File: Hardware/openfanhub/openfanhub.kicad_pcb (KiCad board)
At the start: 2 copper layers, 39.9 x 83.8 mm, 25 parts, among them J1 Conn_01x04_Male, J10 Conn_01x04_Male, J11 Conn_01x04_Male, J12 Conn_01x04_Male, J13 Conn_01x04_Male, J14 Conn_01x04_Male, J15 Conn_01x04_Male, J2 Conn_01x04_Male, J3 Conn_01x04_Male, J4 Conn_01x04_Male, J5 Conn_01x04_Male, J6 Conn_01x04_Male, J7 Conn_01x04_Male, J8 Conn_01x04_Male, J9 Conn_01x04_Male, U1 STM32F103C8T8_Board, U2 AMS1117, U3 USB_HEADER_IN, U4 USB_HEADER_OUT

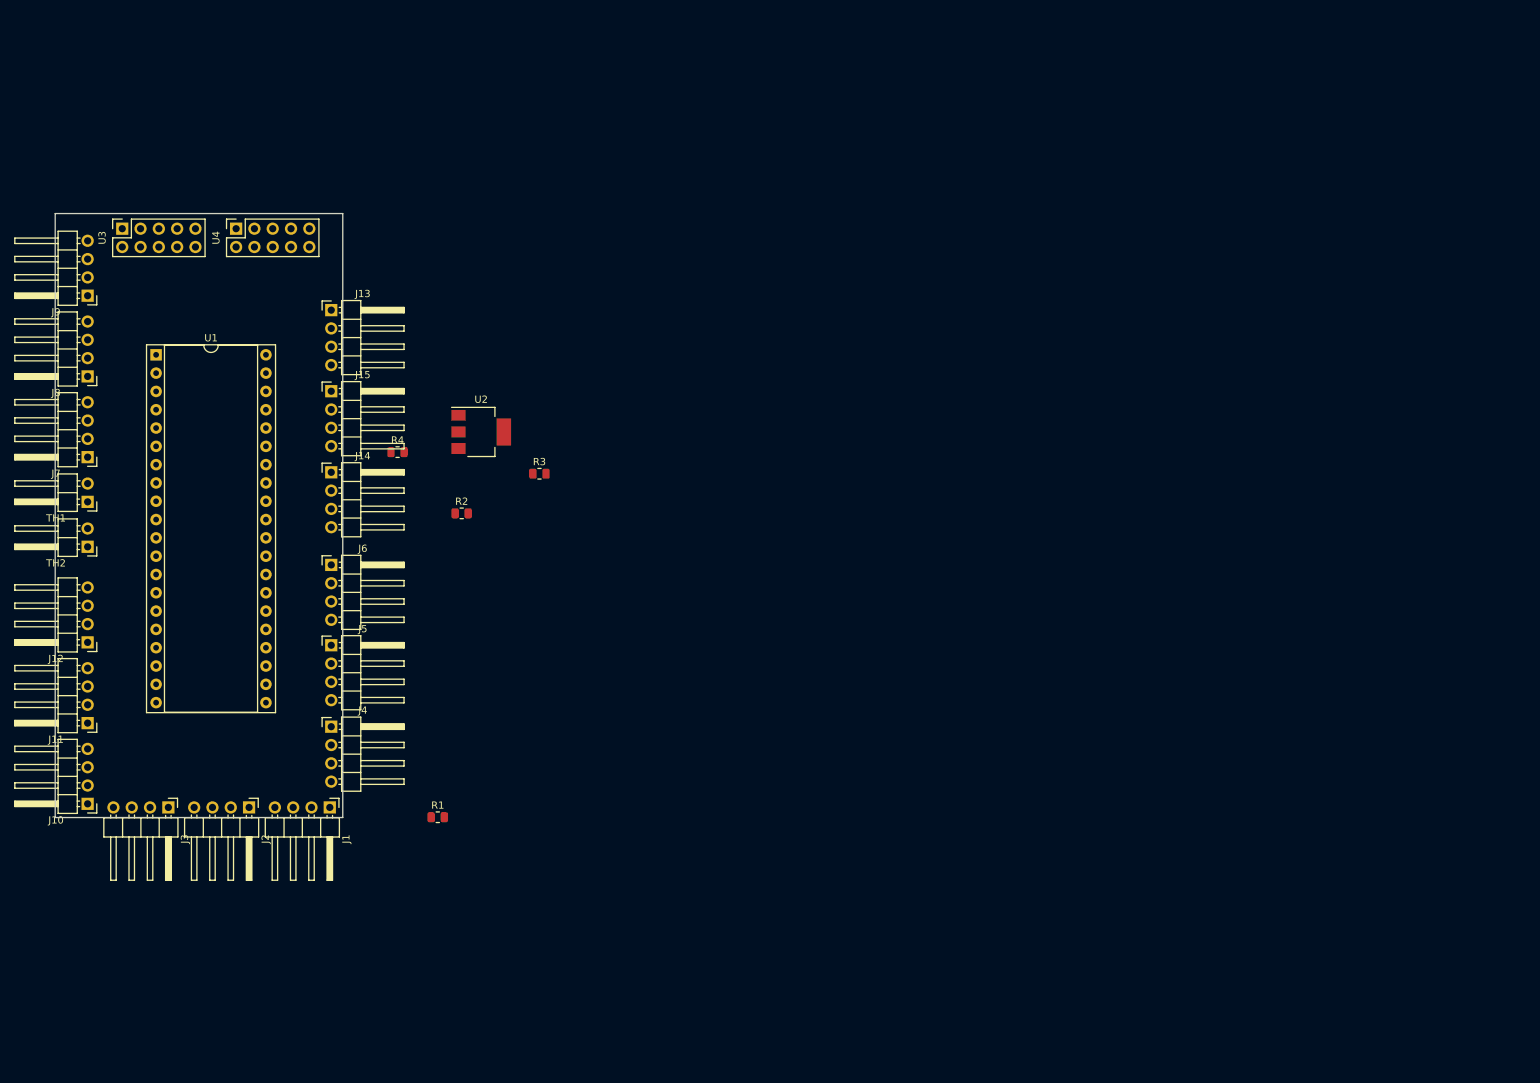
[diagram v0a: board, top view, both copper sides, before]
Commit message: Update files to kicad 6
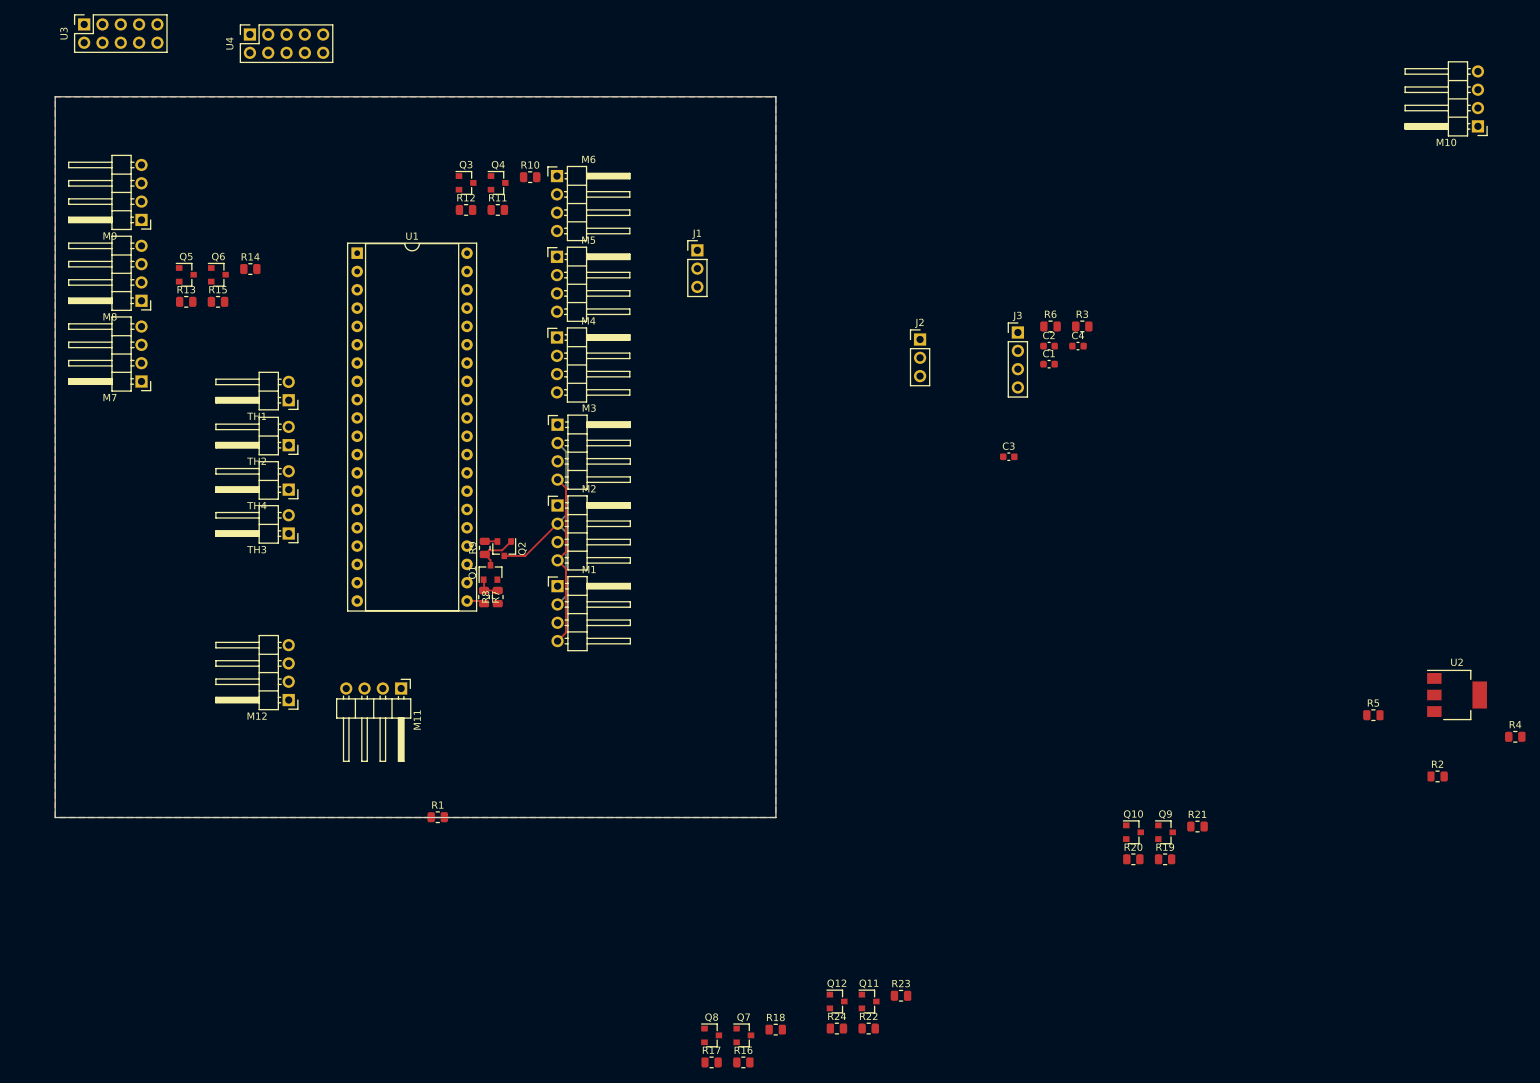
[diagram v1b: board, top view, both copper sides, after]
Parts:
- removed J10, J11, J12, J13, J14, J15, J4, J5, J6, J7, J8, J9: Conn_01x04_Male, Connector_PinHeader_2.54mm:PinHeader_1x04_P2.54mm_Horizontal
- added C1: C, Capacitor_SMD:C_0603_1608Metric, F.Cu at (205.1, 63.4)
- added C2: C, Capacitor_SMD:C_0603_1608Metric, F.Cu at (205.1, 60.9)
- added C3: C, Capacitor_SMD:C_0603_1608Metric, F.Cu at (199.5, 76.2)
- added C4: C, Capacitor_SMD:C_0603_1608Metric, F.Cu at (209.1, 60.9)
- added M1: Fan_4pin, Connector_PinHeader_2.54mm:PinHeader_1x04_P2.54mm_Horizontal, F.Cu at (136.9, 94.2)
- added M10: Fan_4pin, Connector_PinHeader_2.54mm:PinHeader_1x04_P2.54mm_Horizontal, F.Cu at (264.6, 30.4)
- added M11: Fan_4pin, Connector_PinHeader_2.54mm:PinHeader_1x04_P2.54mm_Horizontal, F.Cu at (115.2, 108.4)
- added M12: Fan_4pin, Connector_PinHeader_2.54mm:PinHeader_1x04_P2.54mm_Horizontal, F.Cu at (99.6, 110.0)
- added M2: Fan_4pin, Connector_PinHeader_2.54mm:PinHeader_1x04_P2.54mm_Horizontal, F.Cu at (136.9, 83.0)
- added M3: Fan_4pin, Connector_PinHeader_2.54mm:PinHeader_1x04_P2.54mm_Horizontal, F.Cu at (136.9, 71.8)
- added M4: Fan_4pin, Connector_PinHeader_2.54mm:PinHeader_1x04_P2.54mm_Horizontal, F.Cu at (136.8, 59.7)
- added M5: Fan_4pin, Connector_PinHeader_2.54mm:PinHeader_1x04_P2.54mm_Horizontal, F.Cu at (136.8, 48.5)
- added M6: Fan_4pin, Connector_PinHeader_2.54mm:PinHeader_1x04_P2.54mm_Horizontal, F.Cu at (136.8, 37.3)
- added M7: Fan_4pin, Connector_PinHeader_2.54mm:PinHeader_1x04_P2.54mm_Horizontal, F.Cu at (79.2, 65.8)
- added M8: Fan_4pin, Connector_PinHeader_2.54mm:PinHeader_1x04_P2.54mm_Horizontal, F.Cu at (79.2, 54.6)
- added M9: Fan_4pin, Connector_PinHeader_2.54mm:PinHeader_1x04_P2.54mm_Horizontal, F.Cu at (79.2, 43.4)
- added Q1: Q_NMOS_GSD, Package_TO_SOT_SMD:SOT-23, F.Cu at (127.6, 92.3)
- added Q10: Q_PMOS_GSD, Package_TO_SOT_SMD:SOT-23, F.Cu at (216.8, 128.3)
- added Q11: Q_NMOS_GSD, Package_TO_SOT_SMD:SOT-23, F.Cu at (180.1, 151.8)
- added Q12: Q_PMOS_GSD, Package_TO_SOT_SMD:SOT-23, F.Cu at (175.7, 151.8)
- added Q2: Q_PMOS_GSD, Package_TO_SOT_SMD:SOT-23, F.Cu at (129.5, 89.0)
- added Q3: Q_NMOS_GSD, Package_TO_SOT_SMD:SOT-23, F.Cu at (124.2, 38.2)
- added Q4: Q_PMOS_GSD, Package_TO_SOT_SMD:SOT-23, F.Cu at (128.7, 38.2)
- added Q5: Q_NMOS_GSD, Package_TO_SOT_SMD:SOT-23, F.Cu at (85.4, 51.0)
- added Q6: Q_PMOS_GSD, Package_TO_SOT_SMD:SOT-23, F.Cu at (89.8, 51.0)
- added Q7: Q_NMOS_GSD, Package_TO_SOT_SMD:SOT-23, F.Cu at (162.7, 156.5)
- added Q8: Q_PMOS_GSD, Package_TO_SOT_SMD:SOT-23, F.Cu at (158.3, 156.5)
- added Q9: Q_NMOS_GSD, Package_TO_SOT_SMD:SOT-23, F.Cu at (221.3, 128.3)
- added R10: R, Resistor_SMD:R_0805_2012Metric, F.Cu at (133.1, 37.5)
- added R11: R, Resistor_SMD:R_0805_2012Metric, F.Cu at (128.6, 42.0)
- added R12: R, Resistor_SMD:R_0805_2012Metric, F.Cu at (124.2, 42.0)
- added R13: R, Resistor_SMD:R_0805_2012Metric, F.Cu at (85.4, 54.8)
- added R14: R, Resistor_SMD:R_0805_2012Metric, F.Cu at (94.3, 50.2)
- added R15: R, Resistor_SMD:R_0805_2012Metric, F.Cu at (89.8, 54.8)
- added R16: R, Resistor_SMD:R_0805_2012Metric, F.Cu at (162.7, 160.3)
- added R17: R, Resistor_SMD:R_0805_2012Metric, F.Cu at (158.3, 160.3)
- added R18: R, Resistor_SMD:R_0805_2012Metric, F.Cu at (167.2, 155.7)
- added R19: R, Resistor_SMD:R_0805_2012Metric, F.Cu at (221.2, 132.1)
- added R20: R, Resistor_SMD:R_0805_2012Metric, F.Cu at (216.8, 132.1)
- added R21: R, Resistor_SMD:R_0805_2012Metric, F.Cu at (225.7, 127.5)
- added R22: R, Resistor_SMD:R_0805_2012Metric, F.Cu at (180.1, 155.6)
- added R23: R, Resistor_SMD:R_0805_2012Metric, F.Cu at (184.6, 151.0)
- added R24: R, Resistor_SMD:R_0805_2012Metric, F.Cu at (175.7, 155.6)
- added R3: R, Resistor_SMD:R_0805_2012Metric, F.Cu at (209.7, 58.2)
- added R6: R, Resistor_SMD:R_0805_2012Metric, F.Cu at (205.3, 58.2)
- added R7: R, Resistor_SMD:R_0805_2012Metric, F.Cu at (126.7, 95.7)
- added R8: R, Resistor_SMD:R_0805_2012Metric, F.Cu at (128.6, 95.7)
- added R9: R, Resistor_SMD:R_0805_2012Metric, F.Cu at (126.8, 88.9)
- added TH3: Thermistor, Connector_PinHeader_2.54mm:PinHeader_1x02_P2.54mm_Horizontal, F.Cu at (99.6, 86.9)
- added TH4: Thermistor, Connector_PinHeader_2.54mm:PinHeader_1x02_P2.54mm_Horizontal, F.Cu at (99.6, 80.8)
- J1, J2: value Conn_01x04_Male -> Conn_01x03_Male; footprint Connector_PinHeader_2.54mm:PinHeader_1x04_P2.54mm_Horizontal -> Connector_PinHeader_2.54mm:PinHeader_1x03_P2.54mm_Vertical
- J3: value Conn_01x04_Male -> Conn_01x04_Female; footprint Connector_PinHeader_2.54mm:PinHeader_1x04_P2.54mm_Horizontal -> Connector_PinHeader_2.54mm:PinHeader_1x04_P2.54mm_Vertical
- moved R4 140.2 mm to (269.8, 115.1)
- moved R2 140.2 mm to (259.0, 120.6)
- moved R5 140.2 mm to (250.1, 112.1)
- moved U2 140.2 mm to (261.7, 109.3)
- moved J3 135.0 mm to (200.8, 59.0), turned to 0 degrees
- moved J2 113.5 mm to (187.2, 60.0), turned to 0 degrees
- moved J1 92.6 mm to (156.3, 47.6), turned to 0 degrees
- moved U1 31.3 mm to (109.1, 48.0)
- moved TH1 31.3 mm to (99.6, 68.4)
- moved TH2 31.3 mm to (99.6, 74.6)
- moved U3 28.8 mm to (71.2, 16.3)
- moved U4 27.0 mm to (94.2, 17.7)
- renumbered R3 to R4, R4 to R5
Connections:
- J1 pad 1: +5V -> /UART_RX
- J1 pad 2: /ARGB1 -> /UART_TX
- J1 pad 3: Net-(J1-Pad3) -> GND
- J2 pad 1: +5V -> /SDA
- J2 pad 2: /ARGB2 -> /SCL
- J2 pad 3: Net-(J2-Pad3) -> GND
- J3 pad 1: +5V -> +12V
- J3 pad 2: /ARGB3 -> GND
- J3 pad 3: Net-(J3-Pad3) -> GND
- J3 pad 4: GND -> +5V
- R1 pad 1: /TEMP1_IN -> +5V
- R1 pad 2: GND -> /TEMP1_IN
- R2 pad 1: /TEMP2_IN -> +5V
- R2 pad 2: GND -> /TEMP2_IN
- TH1 pad 1: +5V -> /TEMP1_IN
- TH1 pad 2: /TEMP1_IN -> GND
- TH2 pad 1: +5V -> /TEMP2_IN
- TH2 pad 2: /TEMP2_IN -> GND
- U1 pad 1: Net-(U1-Pad1) -> unconnected-(U1-Pad1)
- U1 pad 11: /FAN3_PWM -> /TEMP3_IN
- U1 pad 12: /FAN3_RPM -> /TEMP4_IN
- U1 pad 13: /FAN4_PWM -> /FAN5_RPM
- U1 pad 14: /FAN4_RPM -> /FAN6_RPM
- U1 pad 15: Net-(U1-Pad15) -> /SCL
- U1 pad 16: Net-(U1-Pad16) -> /SDA
- U1 pad 17: Net-(U1-Pad17) -> unconnected-(U1-Pad17)
- U1 pad 2: Net-(U1-Pad2) -> unconnected-(U1-Pad2)
- U1 pad 21: Net-(U1-Pad21) -> /FAN1_SWITCH
- U1 pad 22: Net-(U1-Pad22) -> /FAN2_SWITCH
- U1 pad 23: Net-(U1-Pad23) -> /FAN3_SWITCH
- U1 pad 24: Net-(U1-Pad24) -> /FAN4_SWITCH
- U1 pad 25: /ARGB1 -> /FAN1_PWM
- U1 pad 26: /ARGB2 -> /FAN2_PWM
- U1 pad 27: /ARGB3 -> unconnected-(U1-Pad27)
- U1 pad 3: Net-(U1-Pad3) -> unconnected-(U1-Pad3)
- U1 pad 30: Net-(U1-Pad30) -> /FAN5_SWITCH
- U1 pad 31: Net-(U1-Pad31) -> /FAN6_SWITCH
- U1 pad 32: Net-(U1-Pad32) -> /FAN3_RPM
- U1 pad 33: Net-(U1-Pad33) -> /FAN4_RPM
- U1 pad 34: /FAN5_RPM -> /FAN3_PWM
- U1 pad 35: /FAN5_PWM -> /FAN4_PWM
- U1 pad 36: /FAN6_RPM -> /FAN5_PWM
- U1 pad 38: Net-(U1-Pad38) -> unconnected-(U1-Pad38)
- U1 pad 4: Net-(U1-Pad4) -> unconnected-(U1-Pad4)
- U1 pad 5: /FAN1_PWM -> /FAN1_RPM
- U1 pad 6: /FAN1_RPM -> /FAN2_RPM
- U1 pad 7: /FAN2_PWM -> /UART_TX
- U1 pad 8: /FAN2_RPM -> /UART_RX
- U3 pad 10: Net-(U3-Pad10) -> unconnected-(U3-Pad10)
- U3 pad 5: Net-(U3-Pad5) -> unconnected-(U3-Pad5)
- U4 pad 10: Net-(U4-Pad10) -> unconnected-(U4-Pad10)
- U4 pad 5: Net-(U4-Pad5) -> unconnected-(U4-Pad5)
- U4 pad 8: Net-(U4-Pad8) -> unconnected-(U4-Pad8)
- U4 pad 9: Net-(U4-Pad9) -> unconnected-(U4-Pad9)
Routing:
- net /PWM_GROUPS/PWM_GROUP1/SWITCHED_POWER: track 0.00 -> 33.6 mm
- net /FAN1_PWM: track 0.00 -> 24.3 mm
- net Net-(Q1-Pad3): track 0.00 -> 6.23 mm
- net Net-(Q1-Pad1): track 0.00 -> 3.42 mm
- net /FAN1_SWITCH: track 0.00 -> 2.51 mm
- net +12V: track 0.00 -> 1.76 mm
- added copper zone on B.Cu, net GND
- added copper zone on F.Cu, net GND
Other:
- board size 39.9 x 83.8 mm -> 100 x 100 mm
- net class Default removed

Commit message: Add first (badly) routed version. Still need to polish it and check all power/signal paths
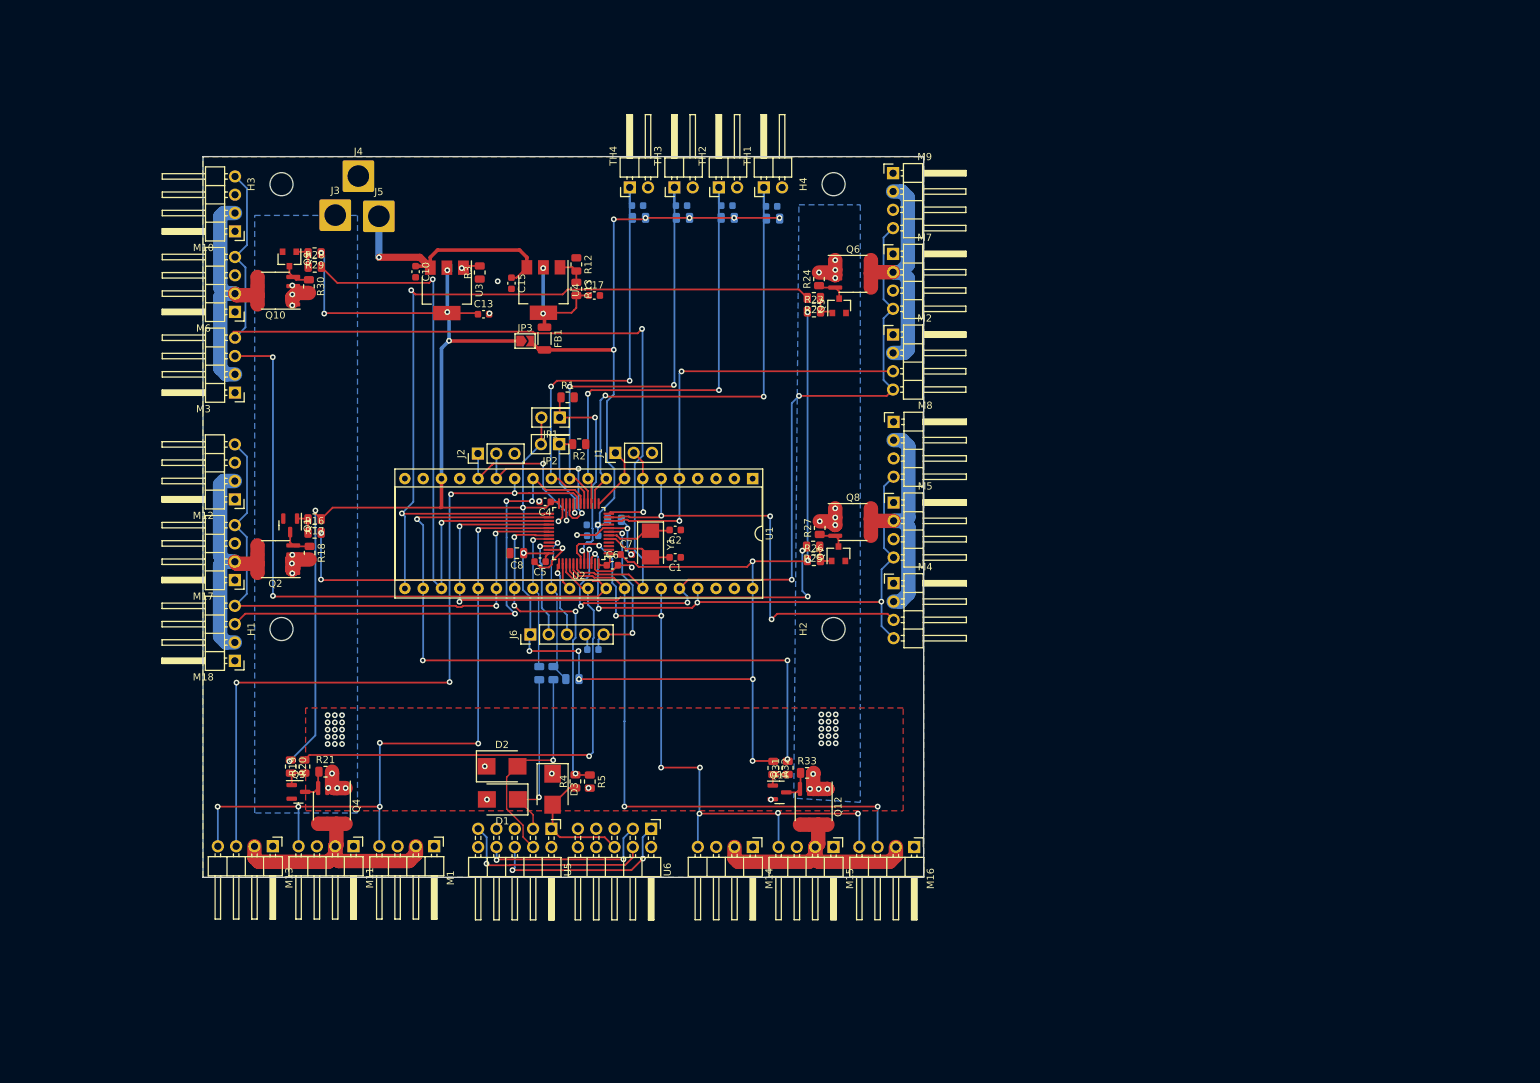
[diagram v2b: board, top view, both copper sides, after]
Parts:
- removed the M10 at (264.6, 30.4)
- removed the Q7 at (162.7, 156.5)
- removed the Q9 at (221.3, 128.3)
- removed the R22 at (180.1, 155.6)
- removed the R23 at (184.6, 151.0)
- removed the R24 at (175.7, 155.6)
- added C1: 22pF, Capacitor_SMD:C_0603_1608Metric, F.Cu at (153.2, 90.2)
- added C10: C, Capacitor_SMD:C_0603_1608Metric, F.Cu at (117.2, 50.6)
- added C11: 10nF, Capacitor_SMD:C_0603_1608Metric, B.Cu at (141.7, 85.7)
- added C12: 10µF, Capacitor_SMD:C_0805_2012Metric, B.Cu at (144.8, 85.0)
- added C13: C, Capacitor_SMD:C_0603_1608Metric, F.Cu at (126.6, 56.5)
- added C15: C, Capacitor_SMD:C_0603_1608Metric, F.Cu at (130.5, 52.2)
- added C17: C, Capacitor_SMD:C_0603_1608Metric, F.Cu at (142.0, 53.9)
- added C2: 22pF, Capacitor_SMD:C_0603_1608Metric, F.Cu at (153.2, 86.4)
- added C3: 100nF, Capacitor_SMD:C_0603_1608Metric, B.Cu at (141.8, 103.0)
- added C4: 100nF, Capacitor_SMD:C_0603_1608Metric, F.Cu at (135.2, 82.5)
- added C5: 100nF, Capacitor_SMD:C_0603_1608Metric, F.Cu at (134.5, 90.8)
- added C6: 100nF, Capacitor_SMD:C_0603_1608Metric, F.Cu at (144.5, 91.3)
- added C7: 100nF, Capacitor_SMD:C_0603_1608Metric, F.Cu at (146.4, 89.8)
- added C8: 10µF, Capacitor_SMD:C_0805_2012Metric, F.Cu at (131.2, 89.6)
- added C9: 100nF, Capacitor_SMD:C_0603_1608Metric, B.Cu at (141.8, 87.2)
- added D1: D_TVS, Diode_SMD:D_SMB, F.Cu at (129.2, 123.8)
- added D2: D_TVS, Diode_SMD:D_SMB, F.Cu at (129.2, 119.2)
- added D3: D_TVS, Diode_SMD:D_SMB, F.Cu at (136.2, 122.4)
- added FB1: FerriteBead, Inductor_SMD:L_1206_3216Metric, F.Cu at (135.1, 59.8)
- added H1: MountingHole, MountingHole:MountingHole_3.2mm_M3, F.Cu at (98.6, 100.1)
- added H2: MountingHole, MountingHole:MountingHole_3.2mm_M3, F.Cu at (175.2, 100.1)
- added H3: MountingHole, MountingHole:MountingHole_3.2mm_M3, F.Cu at (98.6, 38.4)
- added H4: MountingHole, MountingHole:MountingHole_3.2mm_M3, F.Cu at (175.2, 38.4)
- added J4: GND in, Connector_Wire:SolderWire-2.5sqmm_1x01_D2.4mm_OD4.4mm, F.Cu at (109.3, 37.3)
- added J5: 5V IN, Connector_Wire:SolderWire-2.5sqmm_1x01_D2.4mm_OD4.4mm, F.Cu at (112.1, 42.9)
- added J6: SWD, Connector_PinHeader_2.54mm:PinHeader_1x05_P2.54mm_Vertical, F.Cu at (133.1, 100.9)
- added JP1: Jumper_2_Open, Connector_PinHeader_2.54mm:PinHeader_2x01_P2.54mm_Vertical, F.Cu at (137.2, 70.8)
- added JP2: Jumper_2_Open, Connector_PinHeader_2.54mm:PinHeader_2x01_P2.54mm_Vertical, F.Cu at (137.1, 74.5)
- added JP3: 3.3V connect, Jumper:SolderJumper-2_P1.3mm_Open_TrianglePad1.0x1.5mm, F.Cu at (132.4, 60.2)
- added M1: Fan_4pin, Connector_PinHeader_2.54mm:PinHeader_1x04_P2.54mm_Horizontal, F.Cu at (119.8, 130.3)
- added M13: Fan_4pin, Connector_PinHeader_2.54mm:PinHeader_1x04_P2.54mm_Horizontal, F.Cu at (97.4, 130.3)
- added M14: Fan_4pin, Connector_PinHeader_2.54mm:PinHeader_1x04_P2.54mm_Horizontal, F.Cu at (164.0, 130.4)
- added M15: Fan_4pin, Connector_PinHeader_2.54mm:PinHeader_1x04_P2.54mm_Horizontal, F.Cu at (175.2, 130.4)
- added M16: Fan_4pin, Connector_PinHeader_2.54mm:PinHeader_1x04_P2.54mm_Horizontal, F.Cu at (186.4, 130.4)
- added M17: Fan_4pin, Connector_PinHeader_2.54mm:PinHeader_1x04_P2.54mm_Horizontal, F.Cu at (92.1, 93.3)
- added M18: Fan_4pin, Connector_PinHeader_2.54mm:PinHeader_1x04_P2.54mm_Horizontal, F.Cu at (92.1, 104.5)
- added Q1: Q_NMOS_GSD, Package_TO_SOT_SMD:SOT-23, F.Cu at (99.8, 85.8)
- added Q3: Q_NMOS_GSD, Package_TO_SOT_SMD:SOT-23, F.Cu at (100.9, 122.7)
- added R1: 10k, Resistor_SMD:R_0805_2012Metric, F.Cu at (138.3, 68.0)
- added R10: R, Resistor_SMD:R_0805_2012Metric, B.Cu at (136.3, 106.3)
- added R12: R, Resistor_SMD:R_0805_2012Metric, F.Cu at (139.5, 49.6)
- added R13: R, Resistor_SMD:R_0805_2012Metric, F.Cu at (139.5, 53.0)
- added R2: 10k, Resistor_SMD:R_0805_2012Metric, F.Cu at (139.9, 74.5)
- added R31: R, Resistor_SMD:R_0805_2012Metric, F.Cu at (168.8, 119.4)
- added R32: R, Resistor_SMD:R_0805_2012Metric, F.Cu at (166.8, 119.4)
- added R33: R, Resistor_SMD:R_0805_2012Metric, F.Cu at (171.5, 120.1)
- added R4: R, Resistor_SMD:R_0805_2012Metric, F.Cu at (139.4, 121.3)
- added R5: R, Resistor_SMD:R_0805_2012Metric, F.Cu at (141.4, 121.3)
- added R8: R, Resistor_SMD:R_0805_2012Metric, B.Cu at (139.0, 107.1)
- added R9: R, Resistor_SMD:R_0805_2012Metric, B.Cu at (134.4, 106.3)
- added U2: STM32F103C8Tx, Package_QFP:LQFP-48_7x7mm_P0.5mm, F.Cu at (139.8, 86.9)
- added U4: AMS1117, Package_TO_SOT_SMD:SOT-223, F.Cu at (134.9, 53.1)
- added Y1: Crystal, Crystal:Crystal_SMD_5032-2Pin_5.0x3.2mm, F.Cu at (149.8, 88.3)
- C14: renamed from C1; moved to B.Cu
- C16: renamed from C2; moved to B.Cu
- C18: renamed from C3; moved to B.Cu
- C19: renamed from C4; moved to B.Cu
- J1: value Conn_01x03_Male -> UART
- J2: value Conn_01x03_Male -> I2C
- J3: value Conn_01x04_Female -> 12V in; footprint Connector_PinHeader_2.54mm:PinHeader_1x04_P2.54mm_Vertical -> Connector_Wire:SolderWire-2.5sqmm_1x01_D2.4mm_OD4.4mm
- Q10, Q12, Q2, Q4, Q6, Q8: value Q_PMOS_GSD -> AO449; footprint Package_TO_SOT_SMD:SOT-23 -> Package_SO:SOIC-8_3.9x4.9mm_P1.27mm
- R11: renamed from R2; moved to B.Cu
- R14: renamed from R3; moved to B.Cu
- R15: renamed from R6; moved to B.Cu
- R6: renamed from R5; moved to B.Cu
- R7: renamed from R1; moved to B.Cu
- U5: renamed from U3; footprint Connector_PinSocket_2.54mm:PinSocket_2x05_P2.54mm_Vertical -> Connector_PinHeader_2.54mm:PinHeader_2x05_P2.54mm_Horizontal
- U6: renamed from U4; footprint Connector_PinSocket_2.54mm:PinSocket_2x05_P2.54mm_Vertical -> Connector_PinHeader_2.54mm:PinHeader_2x05_P2.54mm_Horizontal
- moved R3 157.5 mm to (126.1, 50.7), turned to 90 degrees
- moved U3 151.0 mm to (121.5, 53.2), turned to -90 degrees
- moved R6 141.7 mm to (122.7, 50.1), turned to 180 degrees
- moved Q10 140.8 mm to (97.8, 53.2), turned to 180 degrees
- moved U5 129.1 mm to (136.0, 127.9), turned to -90 degrees
- moved R11 125.3 mm to (160.5, 43.1), turned to 180 degrees
- moved U6 123.5 mm to (149.9, 127.9), turned to -90 degrees
- moved R21 121.2 mm to (104.7, 119.9)
- moved R19 120.1 mm to (101.8, 119.2), turned to 90 degrees
- moved R20 117.6 mm to (99.9, 119.2), turned to -90 degrees
- moved J3 96.1 mm to (106.1, 42.7)
- moved R7 95.2 mm to (166.8, 43.2), turned to 180 degrees
- moved R16 94.5 mm to (103.2, 86.8)
- moved R17 93.4 mm to (103.2, 84.9), turned to 180 degrees
- moved R18 92.5 mm to (102.5, 89.6), turned to -90 degrees
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- renumbered M9 to M10, M1 to M2, M7 to M3, M8 to M6, M2 to M7, M6 to M8, M3 to M9, Q1 to Q5, Q3 to Q7, Q5 to Q9, R7 to R22, R8 to R23, R9 to R24, R10 to R25, R11 to R26, R12 to R27, R13 to R28, R14 to R29, R4 to R3, R15 to R30, U2 to U3
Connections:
- net Net-(U3-Pad1) renamed /VBUS
- M11 pad 2: /PWM_GROUPS/Fan 5/SWITCHED_POWER -> /PWM_GROUPS/PWM_GROUP6/SWITCHED_POWER
- M11 pad 3: /FAN5_PWM -> /PWM_GROUPS/PWM_GROUP6/Subfan 3/RPM_OUT
- M11 pad 4: /FAN5_RPM -> /FAN6_PWM
- M12 pad 2: /PWM_GROUPS/Fan 6/SWITCHED_POWER -> /PWM_GROUPS/PWM_GROUP5/SWITCHED_POWER
- M12 pad 3: /FAN6_PWM -> /PWM_GROUPS/PWM_GROUP5/Subfan 2/RPM_OUT
- M12 pad 4: /FAN6_RPM -> /FAN5_PWM
- Q10 pad 1: Net-(Q10-Pad1) -> +12V
- Q10 pad 3: /PWM_GROUPS/Fan 5/SWITCHED_POWER -> +12V
- Q12 pad 1: Net-(Q11-Pad3) -> +12V
- Q12 pad 3: /PWM_GROUPS/Fan 6/SWITCHED_POWER -> +12V
- Q2 pad 1: Net-(Q1-Pad3) -> +12V
- Q2 pad 3: /PWM_GROUPS/PWM_GROUP1/SWITCHED_POWER -> +12V
- Q4 pad 1: Net-(Q3-Pad3) -> +12V
- Q4 pad 3: /PWM_GROUPS/PWM_GROUP2/SWITCHED_POWER -> +12V
- Q5 pad 3: Net-(Q1-Pad3) -> Net-(Q5-Pad3)
- Q6 pad 1: Net-(Q5-Pad3) -> +12V
- Q6 pad 3: /PWM_GROUPS/PWM_GROUP3/SWITCHED_POWER -> +12V
- Q7 pad 3: Net-(Q3-Pad3) -> Net-(Q7-Pad3)
- Q8 pad 1: Net-(Q7-Pad3) -> +12V
- Q8 pad 3: /PWM_GROUPS/Fan 4/SWITCHED_POWER -> +12V
- Q9 pad 3: Net-(Q5-Pad3) -> Net-(Q10-Pad4)
- R11 pad 1: +5V -> +3.3VA
- R14 pad 1: +5V -> +3.3VA
- R15 pad 1: +5V -> +3.3VA
- R16 pad 2: /FAN4_SWITCH -> /FAN5_SWITCH
- R17 pad 1: +5V -> +3V3
- R18 pad 1: Net-(Q7-Pad3) -> Net-(Q1-Pad3)
- R19 pad 2: /FAN5_SWITCH -> /FAN6_SWITCH
- R20 pad 1: +5V -> +3V3
- R21 pad 1: Net-(Q10-Pad1) -> Net-(Q3-Pad3)
- R23 pad 1: +5V -> +3V3
- R24 pad 1: Net-(Q1-Pad3) -> Net-(Q5-Pad3)
- R26 pad 1: +5V -> +3V3
- R27 pad 1: Net-(Q3-Pad3) -> Net-(Q7-Pad3)
- R29 pad 1: +5V -> +3V3
- R3 pad 2: Net-(R4-Pad2) -> Net-(R3-Pad2)
- R30 pad 1: Net-(Q5-Pad3) -> Net-(Q10-Pad4)
- R6 pad 1: GND -> Net-(R3-Pad2)
- R7 pad 1: +5V -> +3.3VA
- U1 pad 22: /FAN2_SWITCH -> /FAN4_SWITCH
- U1 pad 24: /FAN4_SWITCH -> /FAN2_SWITCH
- U1 pad 25: /FAN1_PWM -> /FAN6_PWM
- U1 pad 26: /FAN2_PWM -> /FAN5_PWM
- U1 pad 27: unconnected-(U1-Pad27) -> /VBUS_SENSE
- U1 pad 36: /FAN5_PWM -> /FAN1_PWM
- U1 pad 37: /FAN6_PWM -> /FAN2_PWM
- U3 pad 1: Net-(R4-Pad2) -> Net-(R3-Pad2)
- U5 pad 3: /USB_D- -> /D1-
- U5 pad 4: /USB_D+ -> /D1+
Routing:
- net +3V3: track 0.00 -> 316.3 mm, vias 0 -> 17
- net /FAN3_PWM: track 0.00 -> 130.0 mm, vias 0 -> 1
- net /FAN1_SWITCH: track 2.51 -> 118.7 mm, vias 0 -> 2
- net /FAN4_SWITCH: track 0.00 -> 103.0 mm, vias 0 -> 4
- net /FAN6_PWM: track 0.00 -> 101.1 mm, vias 0 -> 6
- net /FAN6_RPM: track 0.00 -> 99.2 mm, vias 0 -> 4
- net /FAN4_PWM: track 0.00 -> 95.8 mm, vias 0 -> 8
- net /FAN3_RPM: track 0.00 -> 92.3 mm, vias 0 -> 2
- net /FAN3_SWITCH: track 0.00 -> 84.1 mm, vias 0 -> 2
- net +3.3VA: track 0.00 -> 84.1 mm, vias 0 -> 7
- net /FAN1_PWM: track 24.3 -> 107.9 mm, vias 0 -> 5
- net /FAN4_RPM: track 0.00 -> 80.1 mm, vias 0 -> 2
- net /FAN5_PWM: track 0.00 -> 79.2 mm, vias 0 -> 2
- net /FAN2_SWITCH: track 0.00 -> 78.3 mm, vias 0 -> 4
- net /FAN2_PWM: track 0.00 -> 75.9 mm, vias 0 -> 4
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- added copper zone on B.Cu, net +12V
- added copper zone on F.Cu, net +12V
